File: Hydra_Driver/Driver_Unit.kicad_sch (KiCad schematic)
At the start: 29 parts, among them IC2 DRV8313RHHR, U3 74HC32, U4 INA199xxDCK, U5 INA199xxDCK

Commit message: Started making some changes based on design review
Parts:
- removed R11, R12, R13, R14, R15, R16: 3.3k, Resistor_SMD:R_0402_1005Metric, symbol Device:R
- removed unit 2 of U3
- removed unit 1 of U3
- removed unit 3 of U3
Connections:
- net IN1H renamed IN1
- net IN2H renamed IN2
- net IN3H renamed IN3

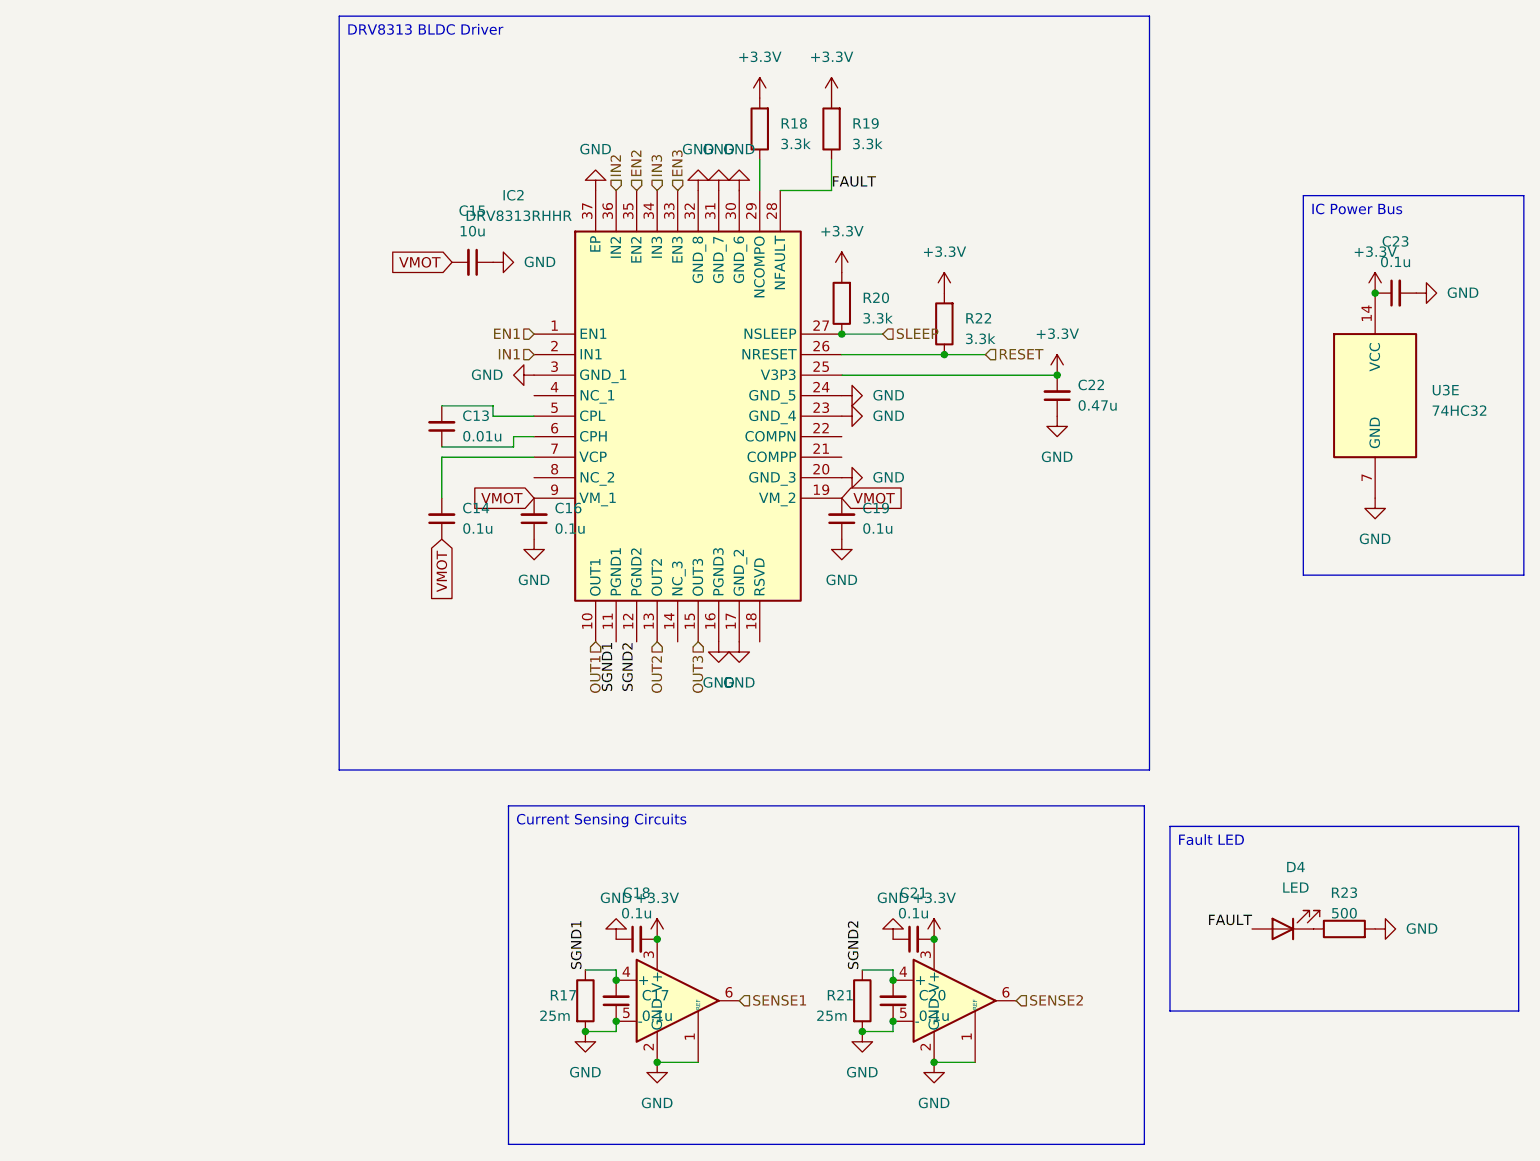
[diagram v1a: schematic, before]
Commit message: Mostly finished applying changes from design review
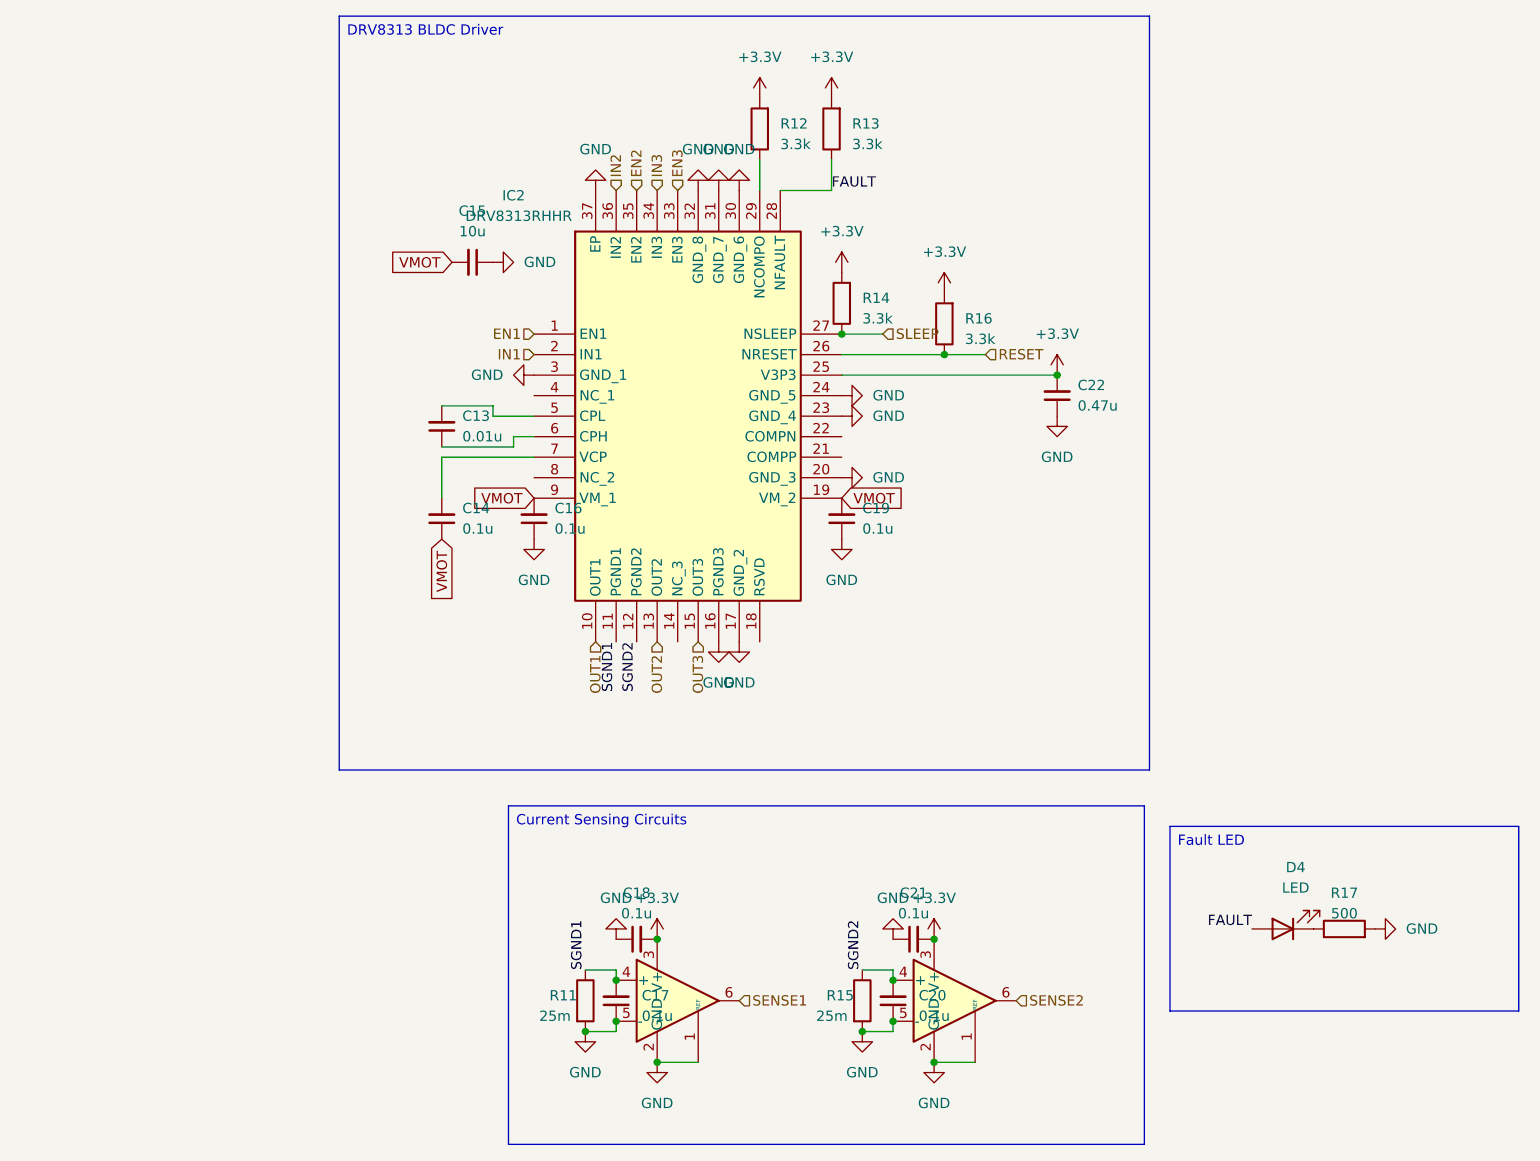
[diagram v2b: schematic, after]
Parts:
- removed C23: 0.1u, Capacitor_SMD:C_0402_1005Metric, symbol Device:C_Small
- removed U3: 74HC32, Package_SO:SOIC-14_3.9x8.7mm_P1.27mm, symbol TacTile:74HC32
- renumbered R17 to R11, R18 to R12, R19 to R13, R20 to R14, R21 to R15, R22 to R16, R23 to R17, U4 to U3, U5 to U4

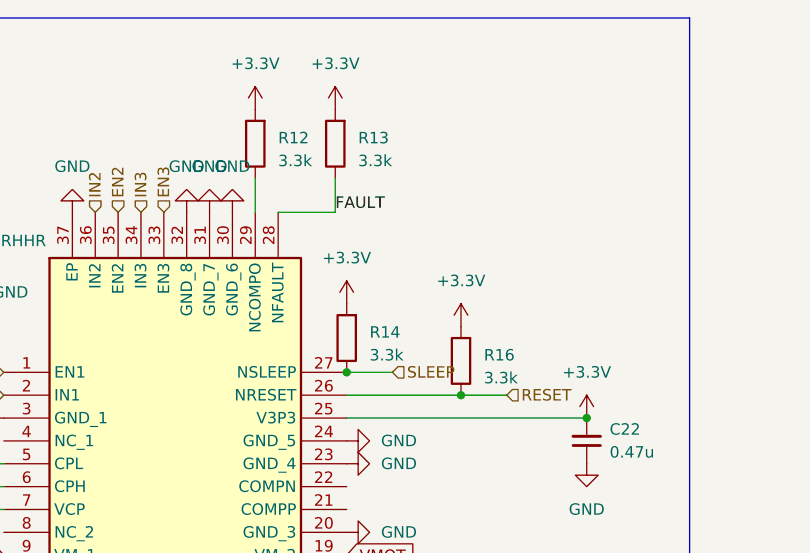
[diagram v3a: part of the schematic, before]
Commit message: Consolidated pullup resistors to 10k
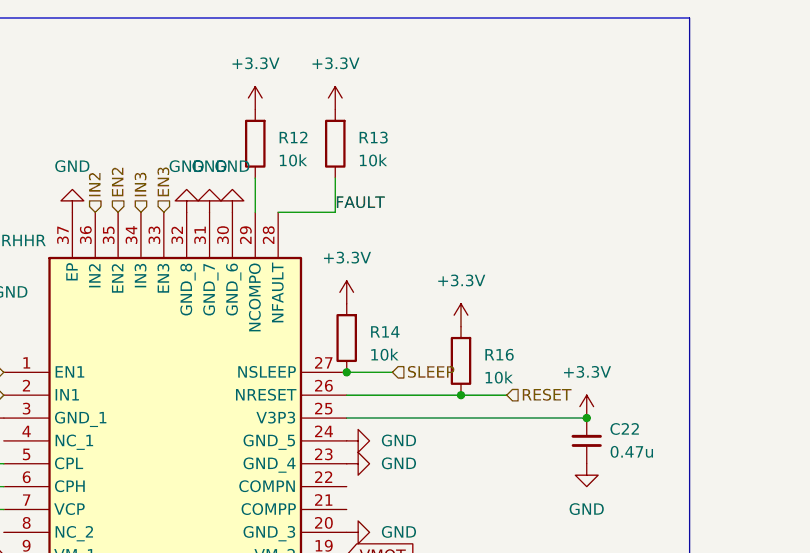
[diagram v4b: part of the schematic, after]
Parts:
- R12, R13, R14, R16: value 3.3k -> 10k
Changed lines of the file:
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@@
 			)
 		)
-		(property "Value" "3.3k"
+		(property "Value" "10k"
 			(at 116.84 48.895 0)
 			(effects
@@
 			)
 		)
-		(property "Value" "3.3k"
+		(property "Value" "10k"
 			(at 106.68 27.305 0)
 			(effects
@@
 			)
 		)
-		(property "Value" "3.3k"
+		(property "Value" "10k"
 			(at 115.57 27.305 0)
 			(effects
@@
 			)
 		)
-		(property "Value" "3.3k"
+		(property "Value" "10k"
 			(at 129.54 51.435 0)
 			(effects
